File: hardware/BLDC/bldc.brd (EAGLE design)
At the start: 51 x 40 mm, 53 parts, among them J1 PWR_2_XT30PW-M, U1 MA702, U2 DRV8323RS, U3 TPN7R006PL, U4 TPN7R006PL, U5 TPN7R006PL, U6 TPN7R006PL, U7 TPN7R006PL, U8 TPN7R006PL, U9 STM32G4_UFQFPN48_T1

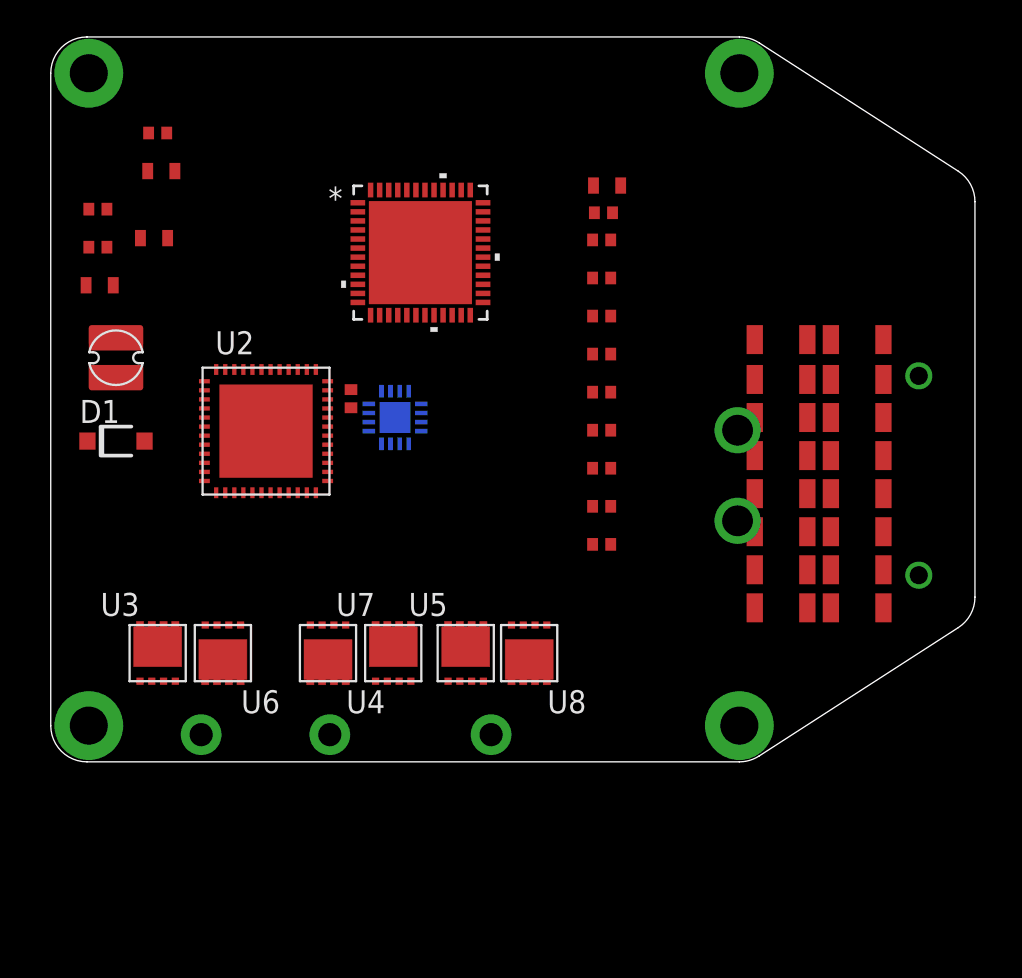
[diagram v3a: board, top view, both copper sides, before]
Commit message: Finishing up DRV8323RS
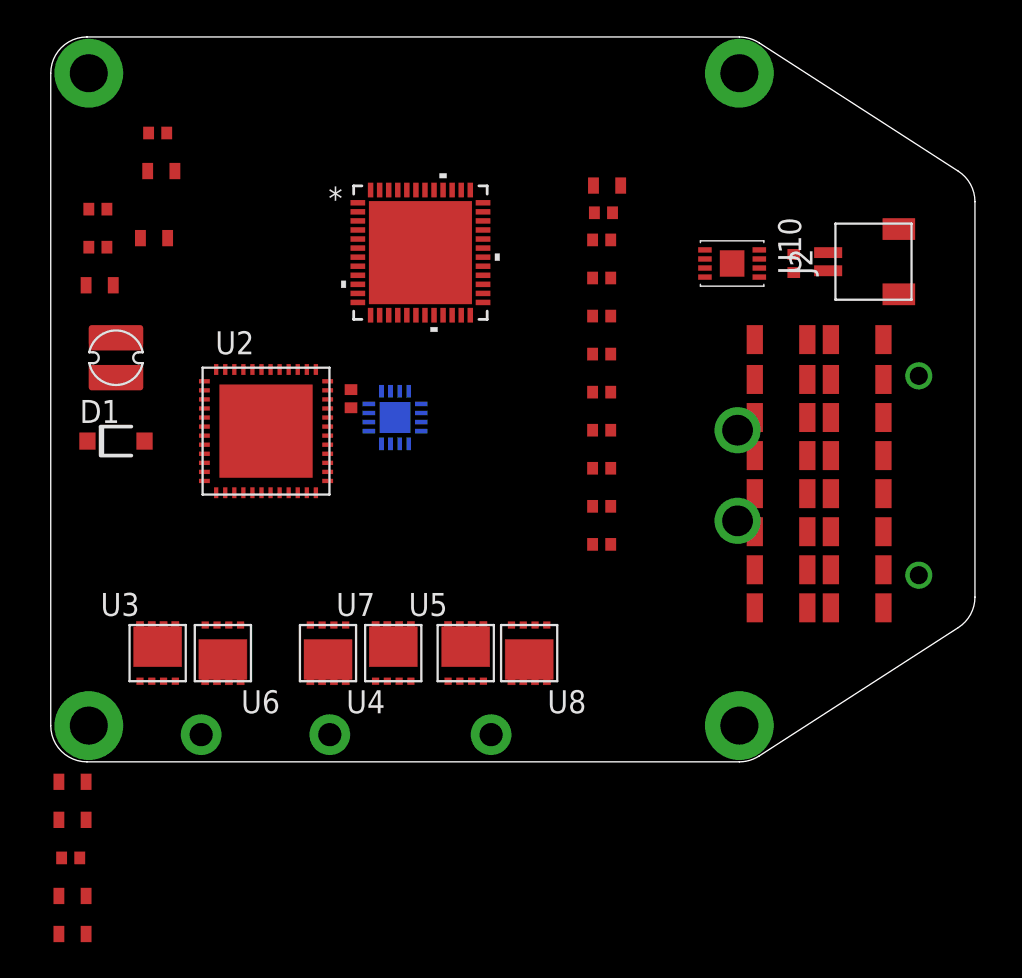
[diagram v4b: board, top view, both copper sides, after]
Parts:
- added C31, C32: 1uf 50v, _T_rcl:C0603
- added C33: 47nF 50v, _T_rcl:C0402
- added C34, C35: 1uf 10v, _T_rcl:C0603
- added J2: LINEAR_2_JST_SH_RA, _T_conn:JST_SM02B-SRSS-TB
- added R4: 120, _T_rcl:R0402
- added U10: MCP2542FD, _T_ic:TDFN_2X3
- C14: value 2.2uF 50V -> 2.2uF 10V
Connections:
- net N$2 renamed SHA
- net N$3 renamed SHB
- net N$4 renamed SHC
- new net 3.3V30MA: C34.1, U2.36
- new net DRV_ENABLE: U2.33, U9.29
- new net GHA: U3.GATE
- new net GHB: U4.GATE
- new net GHC: U5.GATE
- new net GLA: U6.GATE
- new net GLB: U7.GATE
- new net GLC: U8.GATE
- new net N$11: J2.1, R4.2, U10.7
- new net N$12: J2.2, R4.1, U10.6
- new net N$13: C31.2, U2.5
- new net N$14: C33.1, U2.4
- new net N$15: C33.2, U2.3
- new net N$16: U2.15
- new net N$17: U2.20
- new net N$18: U2.11
- new net N$19: U2.14
- new net N$2: U2.8
- new net N$20: U2.21
- new net N$3: U2.17
- new net N$4: U2.18
- new net SPA: U6.SOURCE, U6.SOURCE@1, U6.SOURCE@2
- new net SPB: U7.SOURCE, U7.SOURCE@1, U7.SOURCE@2
- new net SPC: U8.SOURCE, U8.SOURCE@1, U8.SOURCE@2
- new net VCC: C14.1, C35.1, L2.PIN2, R2.2, U10.3, U2.26
- net +24V: now also C31.1, C32.1, U2.6
- net DRV_CS: now also U2.32
- net DRV_MISO: now also U2.29
- net DRV_MOSI: now also U2.30
- net DRV_SCK: now also U2.31
- net GND: now also C32.2, C34.2, C35.2, U2.2, U2.27, U2.35, U2.PAD
- net N$10: now also U2.10; no longer C14.1, L2.PIN2, R2.2

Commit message: Laying out board now
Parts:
- removed C15: 10uF V50, _T_rcl:C1206
- added C36, C41: 0.1uF 10V, _T_rcl:C0402
- added C37, C42: 6.8pF 10V, _T_rcl:C0402
- added C38: 1uF 10V, _T_rcl:C0402
- added C39, C40: 22uF 10V, _T_rcl:C0402
- added GND: 10uF V50, _T_rcl:C1206
- added R10: 150k 1%, _T_rcl:R0402
- added R11: 10k 1%, _T_rcl:R0402
- added R5, R6, R7: 0.001, _T_rcl:R1210_KELVIN
- added R8, R9: 10k, _T_rcl:R0402
- added U11: LDFM33PUR, _T_ic:DFN6_2X2
- added X1: CRYSTAL_NX2016SA-24MHZ-EXS00A-CS11335, _T_ic:NX201SA
- moved C27 41.5 mm to (3.00, 9.90), turned to 270 degrees
- moved C25 38.0 mm to (6.60, 9.90), turned to 270 degrees
- moved C35 36.8 mm to (26.8, 16.9)
- moved C31 35.9 mm to (12.1, 33.1)
- moved C32 35.9 mm to (12.1, 31.0)
- moved C34 35.9 mm to (12.1, 26.8)
- moved C33 35.9 mm to (12.0, 28.9)
- moved C28 35.6 mm to (4.80, 9.90), turned to 270 degrees
- moved C16 34.6 mm to (6.50, 15.7), turned to 0 degrees
- moved C29 23.5 mm to (21.0, 9.80), turned to 270 degrees
- moved C24 16.3 mm to (24.1, 9.80), turned to 270 degrees
- moved C26 14.4 mm to (25.9, 9.80), turned to 270 degrees
- moved C1 6.70 mm to (23.3, 20.1)
- moved U4 4.92 mm to (20.2, 5.60), turned to 0 degrees
- moved U9 3.91 mm to (23.4, 30.6), turned to 90 degrees
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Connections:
- removed net N#8: C1.2, C10.2, C11.2, C12.2, C14.2, C4.2, C5.2, C6.2, C7.2, C8.2, C9.2, D1.A, H1.PAD, H2.PAD, H3.PAD, H4.PAD, R3.1, U1.10, U1.8, U1.PAD, U2.38, U2.40, U2.42, U2.43, U9.49
- removed net N$10: U2.10
- removed net N$16: U2.15
- removed net N$17: U2.20
- removed net N$18: U2.11
- removed net N$19: U2.14
- removed net N$20: U2.21
- removed net N$4: U2.18
- removed net N$7: C2.2, C3.2
- removed net OSC_IN: U9.5
- removed net OSC_OUT: U9.6
- removed net VCC: C14.1, C35.1, L2.PIN2, R2.2, U10.3, U2.26
- new net +5V: C14.1, C36.1, C38.1, L2.PIN2, R2.2, U10.3, U11.PIN5, U11.PIN6
- new net CAL: U2.34
- new net GNDNAME: C1.2, C10.2, C11.2, C12.2, C14.2, C5.2, C6.2, C7.2, C8.2, C9.2, D1.A, R3.1, U1.10, U1.8, U1.PAD, U2.38, U2.40, U2.42, U2.43
- new net N$21: R7.1A, R7.1B, U8.SOURCE, U8.SOURCE@1, U8.SOURCE@2
- new net N$22: R6.1A, R6.1B, U7.SOURCE, U7.SOURCE@1, U7.SOURCE@2
- new net N$23: R5.1A, R5.1B, U6.SOURCE, U6.SOURCE@1, U6.SOURCE@2
- new net NFAULT: R8.1, U2.28
- new net NRST: U9.7
- new net SENSE_A: U2.25, U9.9
- new net SENSE_B: U2.24, U9.8
- new net SENSE_C: U2.23, U9.18
- new net SNA: R5.2_KELVIN, U2.12
- new net SNB: R6.2_KELVIN, U2.13
- new net SNC: R7.2_KELVIN, U2.22
- new net VBUS_SENSE: R10.1, R11.2, U9.25
- new net VDRAIN: U2.7
- net +24V: now also C5.1, GND.1, J1.P$2, R10.2, U3.DRAIN, U4.DRAIN, U5.DRAIN, U9.1; no longer C15.1, J1.P$1
- net +3V3: now also C35.1, C39.1, C40.1, C41.1, R8.2, R9.2, U10.5, U11.PIN1, U2.26; no longer C5.1, U9.1
- net DRV_CS: now also U9.24; no longer U9.25
- net DRV_MISO: now also R9.1
- net FDCAN1_RX: now also U10.4
- net FDCAN1_TX: now also U10.1
- net GHA: now also U2.8
- net GHB: now also U2.17
- net GHC: now also U2.18
- net GLA: now also U2.10
- net GLB: now also U2.15
- net GLC: now also U2.20
- net GND: now also C2.2, C3.2, C36.2, C37.2, C38.2, C39.2, C4.2, C40.2, C41.2, C42.2, GND.2, H1.PAD, H2.PAD, H3.PAD, H4.PAD, J1.P$1, R11.1, R5.2A, R5.2B, R6.2A, R6.2B, R7.2A, R7.2B, U10.2, U10.8, U10.PAD, U11.PAD, U11.PIN4, U9.49, X1.P$2, X1.P$4; no longer C15.2, J1.P$2
- net N$2: now also C37.1, U9.5, X1.P$3; no longer U2.8
- net N$3: now also C42.1, U9.6, X1.P$1; no longer U2.17
- net SHA: now also U2.9
- net SHB: now also U2.16
- net SHC: now also U2.19
- net SPA: now also R5.1_KELVIN, U2.11; no longer U6.SOURCE, U6.SOURCE@1, U6.SOURCE@2
- net SPB: now also R6.1_KELVIN, U2.14; no longer U7.SOURCE, U7.SOURCE@1, U7.SOURCE@2
- net SPC: now also R7.1_KELVIN, U2.21; no longer U8.SOURCE, U8.SOURCE@1, U8.SOURCE@2
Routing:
- net GND: track 0.00 -> 1.20 mm, vias 0 -> 20
- added copper zone on layer 1, net +24V
- added copper zone on layer 15, net +24V
- added copper zone on layer 16, net +24V
- added copper zone on layer 15, net +3V3
- added copper zone on layer 1, net GND
- added copper zone on layer 15, net GND
- added copper zone on layer 16, net GND
- added copper zone on layer 2, net GND
- added copper zone on layer 1, net N$21
- added copper zone on layer 16, net N$21
- added copper zone on layer 1, net N$22
- added copper zone on layer 16, net N$22
- added copper zone on layer 1, net N$23
- added copper zone on layer 16, net N$23
- added copper zone on layer 1, net SHA
- added copper zone on layer 1, net SHB
- added copper zone on layer 1, net SHC

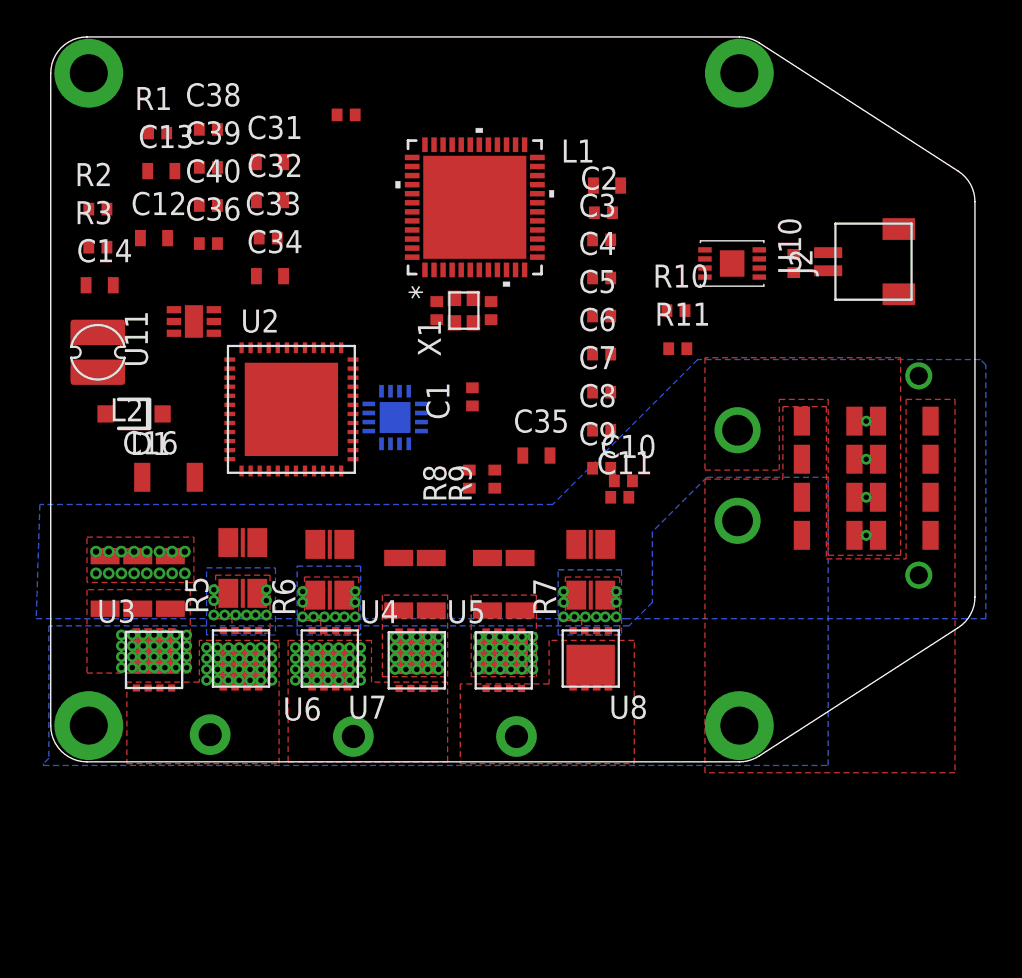
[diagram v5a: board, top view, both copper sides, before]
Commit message: Gonna mess with net classes
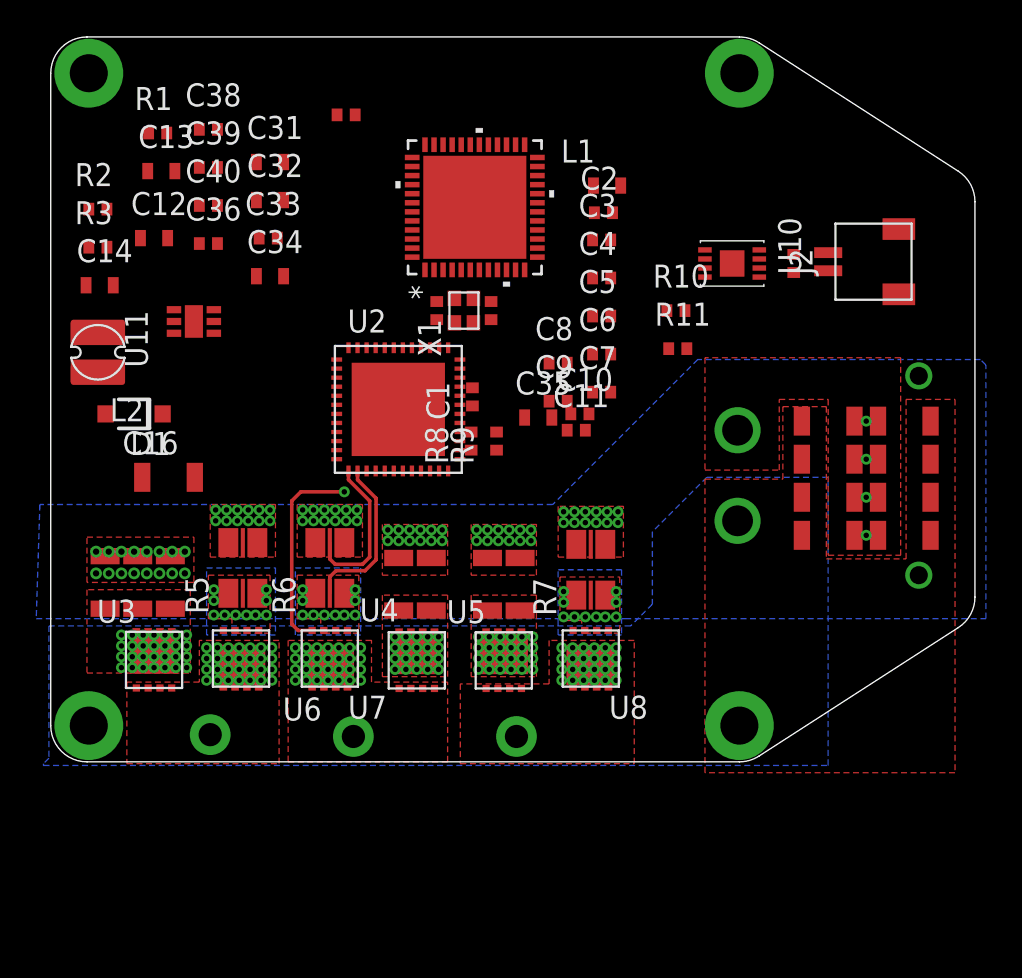
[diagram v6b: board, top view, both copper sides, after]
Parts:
- moved U2 5.90 mm to (19.2, 19.4)
- moved C10 4.41 mm to (29.2, 19.2)
- moved C11 4.41 mm to (29.0, 18.3)
- moved C8 4.41 mm to (28.0, 22.0)
- moved C9 4.41 mm to (28.0, 19.9)
- moved C35 2.10 mm to (26.9, 19.0)
- moved R9 2.10 mm to (24.6, 17.7)
- moved R8 2.10 mm to (23.2, 17.7)
- moved R6 0.10 mm to (15.4, 10.7)
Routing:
- net GLB: track 0.00 -> 11.2 mm, vias 0 -> 1
- net SPB: track 0.00 -> 9.17 mm
- net SNB: track 0.00 -> 8.63 mm
- net GND: vias 20 -> 80

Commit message: Reposition
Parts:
- added J3: LINEAR_8_JST_PH_RA, _T_conn:JST_SM08B-SRSS-TB
- J2: value LINEAR_2_JST_SH_RA -> LINEAR_3_JST_PH_RA; device _T_conn:JST_SM02B-SRSS-TB -> _T_conn:JST_SM03B-SRSS-TB
- moved C36 18.7 mm to (25.1, 37.6), turned to 270 degrees
- moved C32 16.7 mm to (3.60, 16.6)
- moved C31 15.8 mm to (7.30, 18.0), turned to 180 degrees
- moved C9 14.9 mm to (25.2, 34.5), turned to 270 degrees
- moved C4 13.5 mm to (22.1, 16.0)
- moved C6 13.5 mm to (24.3, 34.5), turned to 270 degrees
- moved U10 13.3 mm to (28.8, 37.5)
- moved R4 13.2 mm to (32.4, 37.5)
- moved C41 13.1 mm to (29.4, 34.6)
- moved C12 12.1 mm to (7.30, 16.9), turned to 180 degrees
- moved L1 12.1 mm to (26.0, 20.7), turned to 180 degrees
- moved C5 11.9 mm to (21.2, 32.2)
- moved R1 11.5 mm to (7.40, 23.3), turned to 90 degrees
- moved C7 10.8 mm to (33.3, 30.8), turned to 180 degrees
- moved C33 10.3 mm to (7.30, 19.7)
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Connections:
- removed net GNDNAME: C1.2, C10.2, C11.2, C12.2, C14.2, C5.2, C6.2, C7.2, C8.2, C9.2, D1.A, R3.1, U1.10, U1.8, U1.PAD, U2.38, U2.40, U2.42, U2.43
- net +24V: no longer C5.1, U9.1
- net +3V3: now also C5.1, J3.1, U9.1
- net GND: now also C1.2, C10.2, C11.2, C12.2, C14.2, C5.2, C6.2, C7.2, C8.2, C9.2, D1.A, J2.3, J3.8, R3.1, U1.10, U1.8, U1.PAD, U2.38, U2.40, U2.42, U2.43
- net LPUART1_RX: now also J3.7
- net LPUART1_TX: now also J3.6
- net NRST: now also J3.2
- net SWCLK: now also J3.3
- net SWDIO: now also J3.4
- net SWO: now also J3.5
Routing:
- net GLB: track 11.2 -> 0.00 mm, vias 1 -> 0
- net SPB: track 9.17 -> 0.00 mm
- net SNB: track 8.63 -> 0.00 mm

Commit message: V1 done
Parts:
- moved C36 14.7 mm to (38.7, 32.1), turned to 180 degrees
- moved R4 14.6 mm to (42.0, 26.5)
- moved U10 13.2 mm to (38.7, 28.8), turned to 180 degrees
- moved C41 11.8 mm to (37.4, 25.9)
- moved C4 5.99 mm to (27.1, 19.3), turned to 180 degrees
- moved C1 5.51 mm to (19.6, 21.4), turned to 180 degrees
- moved PHASE_C 3.40 mm to (29.1, 1.40)
- moved R7 3.20 mm to (33.0, 10.7)
- moved U8 3.20 mm to (33.0, 5.80)
- moved C29 3.10 mm to (24.1, 9.90)
- moved GND 3.10 mm to (22.3, 9.90)
- moved U4 3.10 mm to (23.3, 5.70)
- moved PHASE_B 3.10 mm to (19.8, 1.40)
- moved C26 2.40 mm to (28.3, 9.90)
- moved C24 2.40 mm to (26.5, 9.90)
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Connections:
- removed net VDRAIN: U2.7
- net +24V: now also U2.7
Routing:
- net GND: track 1.20 -> 58.4 mm, vias 80 -> 121
- net +5V: track 0.00 -> 56.1 mm, vias 0 -> 2
- net +24V: track 0.00 -> 40.2 mm
- net +3V3: track 0.00 -> 40.1 mm, vias 0 -> 11
- net INHC: track 0.00 -> 30.0 mm, vias 0 -> 2
- net GHC: track 0.00 -> 28.2 mm
- net SWO: track 0.00 -> 27.6 mm, vias 0 -> 2
- net DRV_MISO: track 0.00 -> 26.9 mm, vias 0 -> 2
- net DRV_ENABLE: track 0.00 -> 26.9 mm, vias 0 -> 2
- net INHA: track 0.00 -> 26.5 mm, vias 0 -> 2
- net INHB: track 0.00 -> 26.4 mm, vias 0 -> 2
- net SWDIO: track 0.00 -> 25.9 mm
- net SHC: track 0.00 -> 25.8 mm
- net GLC: track 0.00 -> 25.7 mm
- net SPC: track 0.00 -> 24.6 mm
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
